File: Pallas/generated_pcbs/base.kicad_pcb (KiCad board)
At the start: 2 copper layers, 467.5 x 140 mm, 18 parts

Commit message: Consolidate symbol and fp libraries
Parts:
- removed the MountBaseMiddleTop15 at (526.4, 136.4)
- removed the MountBaseMiddleTop15 at (526.4, 43.9)
- added MountBaseMiddleTop15: MountingHole, Pallas:MountingHole_2.2mm_M2_Pad_Via, F.Cu at (526.4, 136.4)
- added MountBaseMiddleTop15: MountingHole, Pallas:MountingHole_2.2mm_M2_Pad_Via, F.Cu at (526.4, 43.9)
- LogoBase1: footprint keyboard:athena -> Pallas:athena
- LogoBaseMiddleTop: footprint keyboard:Ciaanh_signature -> Pallas:Ciaanh_signature
- MountBaseMiddleTop0, MountBaseMiddleTop10, MountBaseMiddleTop11, MountBaseMiddleTop12, MountBaseMiddleTop13, MountBaseMiddleTop14, MountBaseMiddleTop2, MountBaseMiddleTop3, MountBaseMiddleTop4, MountBaseMiddleTop5, MountBaseMiddleTop6, MountBaseMiddleTop7, MountBaseMiddleTop8, MountBaseMiddleTop9: footprint keyboard:MountingHole_2.2mm_M2_Pad_Via -> Pallas:MountingHole_2.2mm_M2_Pad_Via
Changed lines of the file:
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@@
-(kicad_pcb (version 20171130) (host pcbnew "(5.1.4)-1")
+(kicad_pcb (version 20171130) (host pcbnew 5.1.6-c6e7f7d~86~ubuntu20.04.1)
   (general
     (thickness 1.6)
@@
     (40 Dwgs.User user)
     (41 Cmts.User user)
-    (42 Eco1.User user)
-    (43 Eco2.User user)
+    (42 Eco1.User user hide)
+    (43 Eco2.User user hide)
     (44 Edge.Cuts user)
     (45 Margin user)
@@
       (drillshape 0)
       (scaleselection 1)
-      (outputdirectory "gerber/"))
+      (outputdirectory "pallas/"))
   )
   (net 0 "")
@@
     (uvia_drill 0.1)
   )
-  (module keyboard:Ciaanh_signature (layer F.Cu)
+  (module Pallas:Ciaanh_signature (layer F.Cu)
     (at 72.9496 68.7784 270)
     (fp_text reference LogoBaseMiddleTop (at 0.13 6.04 270) (layer F.SilkS) hide
@@
     )
   )
-  (module keyboard:athena (layer B.Cu)
+  (module Pallas:athena (layer B.Cu)
     (at 289.2496 97.5784 180)
     (fp_text reference LogoBase1 (at 0 0) (layer B.SilkS) hide
@@
       (xy 3.719232 28.550623) (xy 3.751947 29.004353) (xy 3.837836 29.077764) (xy 4.216282 28.987068)) (layer B.SilkS) (width 0.01))
   )
-  (module keyboard:MountingHole_2.2mm_M2_Pad_Via (layer F.Cu)
+  (module Pallas:MountingHole_2.2mm_M2_Pad_Via (layer F.Cu)
     (at 368.8996 48.8784)
     (descr "Mounting Hole 2.2mm, M2")
@@
     (pad 1 thru_hole circle (at 1.166726 -1.166726) (size 0.7 0.7) (drill 0.4) (layers *.Cu *.Mask))
   )
-  (module keyboard:MountingHole_2.2mm_M2_Pad_Via (layer F.Cu)
+  (module Pallas:MountingHole_2.2mm_M2_Pad_Via (layer F.Cu)
     (at 208.8996 48.8784)
     (descr "Mounting Hole 2.2mm, M2")
@@
     (pad 1 thru_hole circle (at 1.166726 -1.166726) (size 0.7 0.7) (drill 0.4) (layers *.Cu *.Mask))
   )
-  (module keyboard:MountingHole_2.2mm_M2_Pad_Via (layer F.Cu)
+  (module Pallas:MountingHole_2.2mm_M2_Pad_Via (layer F.Cu)
     (at 421.3996 136.3784)
     (descr "Mounting Hole 2.2mm, M2")
@@
     (pad 1 thru_hole circle (at 0 0) (size 4.4 4.4) (drill 2.2) (layers *.Cu *.Mask))
   )
-  (module keyboard:MountingHole_2.2mm_M2_Pad_Via (layer F.Cu)
+  (module Pallas:MountingHole_2.2mm_M2_Pad_Via (layer F.Cu)
     (at 121.3996 136.3784)
     (descr "Mounting Hole 2.2mm, M2")
@@
     (pad 1 thru_hole circle (at 0 0) (size 4.4 4.4) (drill 2.2) (layers *.Cu *.Mask))
   )
-  (module keyboard:MountingHole_2.2mm_M2_Pad_Via (layer F.Cu)
+  (module Pallas:MountingHole_2.2mm_M2_Pad_Via (layer F.Cu)
     (at 448.918 80.1114)
     (descr "Mounting Hole 2.2mm, M2")
@@
     (pad 1 thru_hole circle (at 0 0) (size 4.4 4.4) (drill 2.2) (layers *.Cu *.Mask))
   )
-  (module keyboard:MountingHole_2.2mm_M2_Pad_Via (layer F.Cu)
+  (module Pallas:MountingHole_2.2mm_M2_Pad_Via (layer F.Cu)
     (at 128.818 80.1114)
     (descr "Mounting Hole 2.2mm, M2")
@@
     (pad 1 thru_hole circle (at 0 0) (size 4.4 4.4) (drill 2.2) (layers *.Cu *.Mask))
   )
-  (module keyboard:MountingHole_2.2mm_M2_Pad_Via (layer F.Cu)
+  (module Pallas:MountingHole_2.2mm_M2_Pad_Via (layer F.Cu)
     (at 368.8488 92.8784)
     (descr "Mounting Hole 2.2mm, M2")
@@
     (pad 1 thru_hole circle (at 0 0) (size 4.4 4.4) (drill 2.2) (layers *.Cu *.Mask))
   )
-  (module keyboard:MountingHole_2.2mm_M2_Pad_Via (layer F.Cu)
+  (module Pallas:MountingHole_2.2mm_M2_Pad_Via (layer F.Cu)
     (at 208.8488 92.8784)
     (descr "Mounting Hole 2.2mm, M2")
@@
     (pad 1 thru_hole circle (at 0 0) (size 4.4 4.4) (drill 2.2) (layers *.Cu *.Mask))
   )
-  (module keyboard:MountingHole_2.2mm_M2_Pad_Via (layer F.Cu)
+  (module Pallas:MountingHole_2.2mm_M2_Pad_Via (layer F.Cu)
     (at 316.3996 45.8784)
     (descr "Mounting Hole 2.2mm, M2")
@@
     (pad 1 thru_hole circle (at 0 0) (size 4.4 4.4) (drill 2.2) (layers *.Cu *.Mask))
   )
-  (module keyboard:MountingHole_2.2mm_M2_Pad_Via (layer F.Cu)
+  (module Pallas:MountingHole_2.2mm_M2_Pad_Via (layer F.Cu)
     (at 261.3996 45.8784)
     (descr "Mounting Hole 2.2mm, M2")
@@
     (pad 1 thru_hole circle (at 0 0) (size 4.4 4.4) (drill 2.2) (layers *.Cu *.Mask))
   )
-  (module keyboard:MountingHole_2.2mm_M2_Pad_Via (layer F.Cu)
+  (module Pallas:MountingHole_2.2mm_M2_Pad_Via (layer F.Cu)
     (at 248.8488 147.8784)
     (descr "Mounting Hole 2.2mm, M2")
@@
     (pad 1 thru_hole circle (at 0 0) (size 4.4 4.4) (drill 2.2) (layers *.Cu *.Mask))
   )
-  (module keyboard:MountingHole_2.2mm_M2_Pad_Via (layer F.Cu)
+  (module Pallas:MountingHole_2.2mm_M2_Pad_Via (layer F.Cu)
     (at 328.8488 147.8784)
     (descr "Mounting Hole 2.2mm, M2")
@@
     (pad 1 thru_hole circle (at 0 0) (size 4.4 4.4) (drill 2.2) (layers *.Cu *.Mask))
   )
-  (module keyboard:MountingHole_2.2mm_M2_Pad_Via (layer F.Cu)
+  (module Pallas:MountingHole_2.2mm_M2_Pad_Via (layer F.Cu)
     (at 526.3996 136.3784)
     (descr "Mounting Hole 2.2mm, M2")
@@
     (pad 1 thru_hole circle (at 0 0) (size 4.4 4.4) (drill 2.2) (layers *.Cu *.Mask))
   )
-  (module keyboard:MountingHole_2.2mm_M2_Pad_Via (layer F.Cu)
+  (module Pallas:MountingHole_2.2mm_M2_Pad_Via (layer F.Cu)
     (at 526.3996 43.8784)
     (descr "Mounting Hole 2.2mm, M2")
@@
     (pad 1 thru_hole circle (at 0 0) (size 4.4 4.4) (drill 2.2) (layers *.Cu *.Mask))
   )
-  (module keyboard:MountingHole_2.2mm_M2_Pad_Via (layer F.Cu)
+  (module Pallas:MountingHole_2.2mm_M2_Pad_Via (layer F.Cu)
     (at 68.8996 136.3784)
     (descr "Mounting Hole 2.2mm, M2")
@@
     (pad 1 thru_hole circle (at 0 0) (size 4.4 4.4) (drill 2.2) (layers *.Cu *.Mask))
   )
-  (module keyboard:MountingHole_2.2mm_M2_Pad_Via (layer F.Cu)
+  (module Pallas:MountingHole_2.2mm_M2_Pad_Via (layer F.Cu)
     (at 68.8996 43.8784)
     (descr "Mounting Hole 2.2mm, M2")

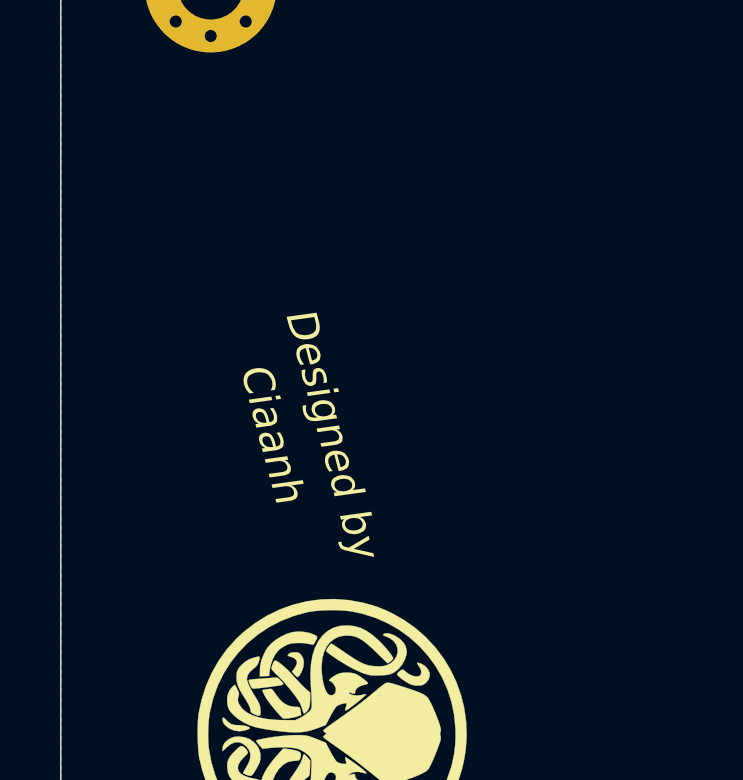
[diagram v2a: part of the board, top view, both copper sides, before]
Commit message: rev 0.2 fix diode an res position with stabs
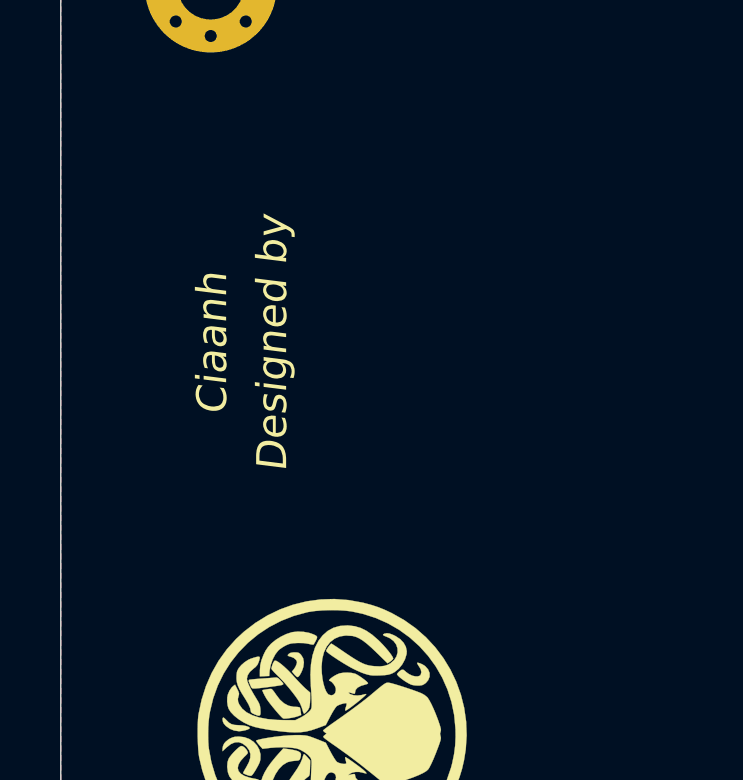
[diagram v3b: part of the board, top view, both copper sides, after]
